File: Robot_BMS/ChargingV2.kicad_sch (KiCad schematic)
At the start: 11 parts, among them Q1 2N7002, U1 TPS54308DDCR

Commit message: mid way implementing new usb-pd chip
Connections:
- net VBUS renamed USB_C
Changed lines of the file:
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@@
 		)
 	)
-	(hierarchical_label "VBUS"
+	(hierarchical_label "USB_C"
 		(shape output)
 		(at 237.49 96.52 0)

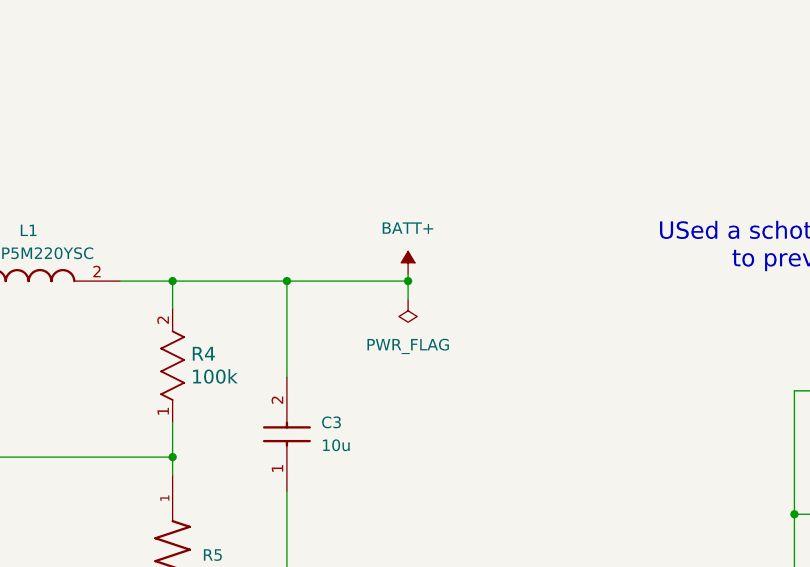
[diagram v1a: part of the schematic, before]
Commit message: PCB layout up to charging circuit
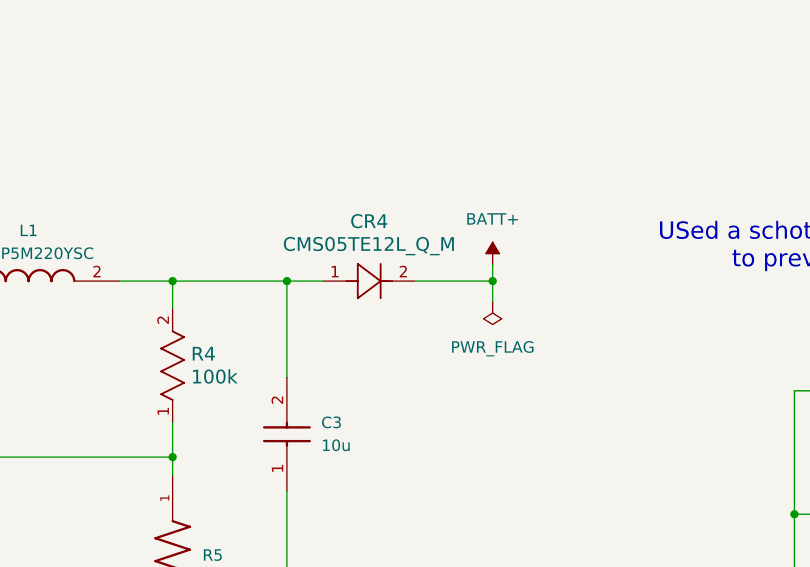
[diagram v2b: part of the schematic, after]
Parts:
- added CR4: CMS05TE12L_Q_M, RobotBMS:M-FLAT_TOS, symbol Toshiba schottky diode:CMS05TE12L_Q_M
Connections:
- net BATT+: now also CR4.2; no longer C3.2, L1.2, R4.2
- new net: C3.2, CR4.1, L1.2, R4.2
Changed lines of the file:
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@@
+	)
+	(junction
+		(at 150.114 70.612)
+		(diameter 0)
+		(color 0 0 0 0)
+	)
+	(junction
+		(at 172.974 70.612)
+		(diameter 0)
+		(color 0 0 0 0)
 	)
 	(junction
@@
 	)
 	(junction
-		(at 163.576 70.612)
-		(diameter 0)
-		(color 0 0 0 0)
-	)
-	(junction
 		(at 32.766 61.214)
 		(diameter 0)
@@
 	)
 	(junction
-		(at 150.114 70.612)
-		(diameter 0)
-		(color 0 0 0 0)
-	)
-	(junction
 		(at 72.39 61.214)
 		(diameter 0)
@@
 	(wire
 		(pts
-			(xy 163.576 70.612) (xy 163.576 69.85)
+			(xy 172.974 68.834) (xy 172.974 70.612)
 		)
 		(stroke
@@
 	(wire
 		(pts
+			(xy 172.974 70.612) (xy 172.974 72.898)
+		)
+		(stroke
+			(width 0)
+			(type default)
+		)
+	)
+	(wire
+		(pts
 			(xy 98.806 73.152) (xy 98.806 90.17)
 		)
@@
 	(wire
 		(pts
-			(xy 150.114 70.612) (xy 163.576 70.612)
-		)
-		(stroke
-			(width 0)
-			(type default)
-		)
-	)
-	(wire
-		(pts
 			(xy 78.486 61.214) (xy 78.486 68.072)
 		)
@@
 	(wire
 		(pts
+			(xy 164.338 70.612) (xy 172.974 70.612)
+		)
+		(stroke
+			(width 0)
+			(type default)
+		)
+	)
+	(wire
+		(pts
 			(xy 206.502 82.804) (xy 206.502 96.52)
 		)
@@
 	(wire
 		(pts
-			(xy 163.576 72.644) (xy 163.576 70.612)
-		)
-		(stroke
-			(width 0)
-			(type default)
-		)
-	)
-	(wire
-		(pts
 			(xy 137.414 86.36) (xy 137.414 90.17)
 		)
@@
 	(wire
 		(pts
+			(xy 137.414 70.612) (xy 150.114 70.612)
+		)
+		(stroke
+			(width 0)
+			(type default)
+		)
+	)
+	(wire
+		(pts
+			(xy 150.114 70.612) (xy 154.178 70.612)
+		)
+		(stroke
+			(width 0)
+			(type default)
+		)
+	)
+	(wire
+		(pts
 			(xy 32.766 61.214) (xy 72.39 61.214)
 		)
@@
 		(pts
 			(xy 32.766 61.214) (xy 32.766 71.12)
-		)
-		(stroke
-			(width 0)
-			(type default)
-		)
-	)
-	(wire
-		(pts
-			(xy 137.414 70.612) (xy 150.114 70.612)
 		)
 		(stroke
@@
 	)
 	(symbol
+		(lib_id "Toshiba schottky diode:CMS05TE12L_Q_M")
+		(at 164.338 70.612 180)
+		(unit 1)
+		(exclude_from_sim no)
+		(in_bom yes)
+		(on_board yes)
+		(dnp no)
+		(fields_autoplaced yes)
+		(property "Reference" "CR4"
+			(at 159.258 64.008 0)
+			(effects
+				(font
+					(size 1.524 1.524)
+				)
+			)
+		)
+		(property "Value" "CMS05TE12L_Q_M"
+			(at 159.258 66.548 0)
+			(effects
+				(font
+					(size 1.524 1.524)
+				)
+			)
+		)
+		(property "Footprint" "RobotBMS:M-FLAT_TOS"
+			(at 164.338 70.612 0)
+			(effects
+				(font
+					(size 1.27 1.27)
+					(italic yes)
+				)
+				(hide yes)
+			)
+		)
+		(property "Datasheet" "https://www.mouser.co.uk/ProductDetail/Toshiba/CMS05TE12LQM?qs=JiHARDETuZDcvazKO1MDNQ%3D%3D&srsltid=AfmBOopWrxi0PKcgDv_hck6b5GzUq4xcRRzPONvEurGhtaMTFZsmDRz3"
+			(at 164.338 70.612 0)
+			(effects
+				(font
+					(size 1.27 1.27)
+					(italic yes)
+				)
+				(hide yes)
+			)
+		)
+		(property "Description" "Schottky Diode 0.45V FWD Voltage"
+			(at 164.338 70.612 0)
+			(effects
+				(font
+					(size 1.27 1.27)
+				)
+				(hide yes)
+			)
+		)
+		(property "Price" "0.80"
+			(at 164.338 70.612 0)
+			(effects
+				(font
+					(size 1.27 1.27)
+				)
+				(hide yes)
+			)
+		)
+		(property "Manufacturer_Part_Number" "CMS05TE12L_Q_M"
+			(at 164.338 70.612 0)
+			(effects
+				(font
+					(size 1.27 1.27)
+				)
+				(hide yes)
+			)
+		)
+		(pin "2"
+		)
+		(pin "1"
+		)
+		(instances
+			(project "Robot_BMS"
+				(path "/72551b1c-3d40-4199-8911-e5b015f4abec/31837631-dd5f-49d4-a8ae-a36c80dc2ea1"
+					(reference "CR4")
+					(unit 1)
+				)
+			)
+		)
+	)
+	(symbol
 		(lib_id "power:-BATT")
-		(at 163.576 69.85 0)
+		(at 172.974 68.834 0)
 		(unit 1)
 		(exclude_from_sim no)
@@
 		(fields_autoplaced yes)
 		(property "Reference" "#PWR07"
-			(at 163.576 73.66 0)
+			(at 172.974 72.644 0)
 			(effects
 				(font
@@
 		)
 		(property "Value" "BATT+"
-			(at 163.576 64.77 0)
+			(at 172.974 63.754 0)
 			(effects
 				(font
@@
 		)
 		(property "Footprint" ""
-			(at 163.576 69.85 0)
+			(at 172.974 68.834 0)
 			(effects
 				(font
@@
 		)
 		(property "Datasheet" ""
-			(at 163.576 69.85 0)
+			(at 172.974 68.834 0)
 			(effects
 				(font
@@
 		)
 		(property "Description" "Power symbol creates a global label with name \"-BATT\""
-			(at 163.576 69.85 0)
+			(at 172.974 68.834 0)
 			(effects
 				(font
@@
 	(symbol
 		(lib_id "power:PWR_FLAG")
-		(at 163.576 72.644 180)
+		(at 172.974 72.898 180)
 		(unit 1)
 		(exclude_from_sim no)
@@
 		(dnp no)
 		(property "Reference" "#FLG04"
-			(at 163.576 74.549 0)
+			(at 172.974 74.803 0)
 			(effects
 				(font
@@
 		)
 		(property "Value" "PWR_FLAG"
-			(at 163.576 77.724 0)
+			(at 172.974 77.978 0)
 			(effects
 				(font
@@
 		)
 		(property "Footprint" ""
-			(at 163.576 72.644 0)
+			(at 172.974 72.898 0)
 			(effects
 				(font
@@
 		)
 		(property "Datasheet" "~"
-			(at 163.576 72.644 0)
+			(at 172.974 72.898 0)
 			(effects
 				(font
@@
 		)
 		(property "Description" "Special symbol for telling ERC where power comes from"
-			(at 163.576 72.644 0)
-			(effects
-				(font
+			(at 172.974 72.898 0)
+			(effects
+				(font

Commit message: halfway throgh battery management pcb layout
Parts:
- renumbered CR4 to CR1, CR1 to CR2, CR2 to CR3, CR3 to CR4
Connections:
- net BATT+ renamed TO_LOAD

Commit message: manufacture ready
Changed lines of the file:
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@@
 (kicad_sch
-	(version 20231120)
+	(version 20250114)
 	(generator "eeschema")
-	(generator_version "8.0")
+	(generator_version "9.0")
 	(paper "A4")
+	(text "helpful link"
+		(exclude_from_sim no)
+		(at 260.096 149.098 0)
+		(effects
+			(font
+				(size 1.905 1.905)
+			)
+			(href "https://webench.ti.com/power-designer/switching-regulator/customize/12?noparams=0")
+		)
+	)
+	(text "Charges @ 13V 1A and is fed either by \nthe USB-C or DC Barrel Jack supply\nor Solar Power"
+		(exclude_from_sim no)
+		(at 82.042 39.624 0)
+		(effects
+			(font
+				(size 2.54 2.54)
+			)
+		)
+	)
+	(text "USed a schottky diode with max fw volt drop of 0.45V\nto prevent voltages from going upstream"
+		(exclude_from_sim no)
+		(at 226.568 66.802 0)
+		(effects
+			(font
+				(size 1.905 1.905)
+			)
+		)
+	)
+	(text "15V to 28V DC In\n13V @ 1A OUT"
+		(exclude_from_sim no)
+		(at 72.39 118.618 0)
+		(effects
+			(font
+				(size 2.54 2.54)
+			)
+		)
+	)
+	(text "3S Li+ Ion Charger"
+		(exclude_from_sim no)
+		(at 82.55 22.606 0)
+		(effects
+			(font
+				(size 7.62 7.62)
+			)
+		)
+	)
+	(text "All standard Passive\ncomponenets are 0603 imperial"
+		(exclude_from_sim no)
+		(at 208.28 173.736 0)
+		(effects
+			(font
+				(size 2.54 2.54)
+			)
+		)
+	)
 	(junction
 		(at 137.414 116.586)
@@
 		)
 	)
-	(text "helpful link"
-		(exclude_from_sim no)
-		(at 260.096 149.098 0)
-		(effects
-			(font
-				(size 1.905 1.905)
-			)
-			(href "https://webench.ti.com/power-designer/switching-regulator/customize/12?noparams=0")
-		)
-	)
-	(text "Charges @ 13V 1A and is fed either by \nthe USB-C or DC Barrel Jack supply\nor Solar Power"
-		(exclude_from_sim no)
-		(at 82.042 39.624 0)
-		(effects
-			(font
-				(size 2.54 2.54)
-			)
-		)
-	)
-	(text "USed a schottky diode with max fw volt drop of 0.45V\nto prevent voltages from going upstream"
-		(exclude_from_sim no)
-		(at 226.568 66.802 0)
-		(effects
-			(font
-				(size 1.905 1.905)
-			)
-		)
-	)
-	(text "15V to 28V DC In\n13V @ 1A OUT"
-		(exclude_from_sim no)
-		(at 72.39 118.618 0)
-		(effects
-			(font
-				(size 2.54 2.54)
-			)
-		)
-	)
-	(text "3S Li+ Ion Charger"
-		(exclude_from_sim no)
-		(at 82.55 22.606 0)
-		(effects
-			(font
-				(size 7.62 7.62)
-			)
-		)
-	)
-	(text "All standard Passive\ncomponenets are 0603 imperial"
-		(exclude_from_sim no)
-		(at 208.28 173.736 0)
-		(effects
-			(font
-				(size 2.54 2.54)
-			)
-		)
-	)
